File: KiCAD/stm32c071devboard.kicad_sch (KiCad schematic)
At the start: 24 parts, among them J1 USB_C_Receptacle_USB2.0_14P, J2 Conn_01x14_Pin, J3 Conn_01x01_Pin, J4 Conn_01x14_Pin, J5 Conn_01x02_Pin, U1 STM32C071G8UxN, U3 TPS73633DBV

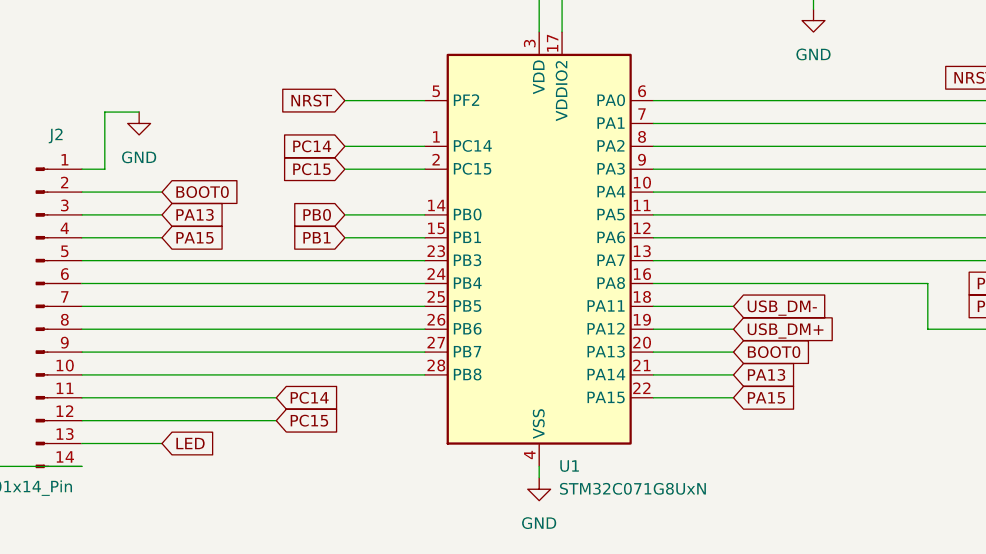
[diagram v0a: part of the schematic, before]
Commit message: Fixed 2 pins
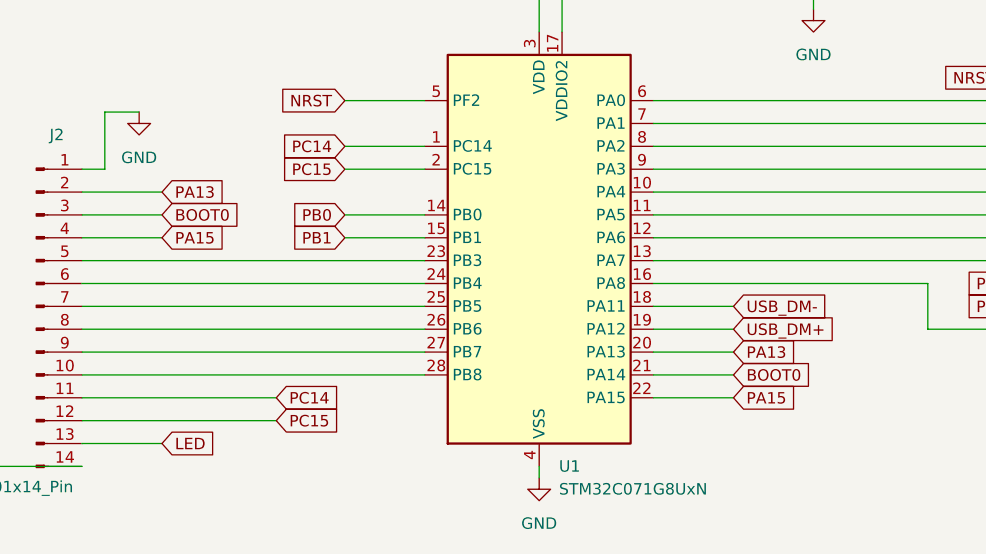
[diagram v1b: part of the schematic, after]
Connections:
- net BOOT0: now also J2.3 (Pin_3), U1.21 (PA14); no longer J2.2 (Pin_2), U1.20 (PA13)
- net PA13: now also J2.2 (Pin_2), U1.20 (PA13); no longer J2.3 (Pin_3), U1.21 (PA14)
